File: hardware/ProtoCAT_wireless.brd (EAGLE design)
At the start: 59.7 x 53.3 mm, 69 parts, among them Q1 MOSFET-NCHANNELSMD, Q2 MOSFET-NCHANNELSMD, U1 ARDUINO, U3 TB6612FNG

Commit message: Numerous minor edits
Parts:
- added F3: PTCSMD, SparkFun-PowerIC:PTC-1206
- moved C2 20.7 mm to (30.5, 10.8), turned to 180 degrees
- moved FRAME1 15.3 mm to (-3.81, -10.2)
- moved LOGO4 7.41 mm to (58.4, 31.8)
- moved LOGO3 5.03 mm to (5.21, 1.52), turned to 0 degrees
- moved SJ2 3.95 mm to (33.1, 14.7), turned to 90 degrees
- moved LOGO1 2.84 mm to (14.9, 4.32)
- moved JP20 1.27 mm to (21.6, 8.00)
- moved C4 0.32 mm to (34.0, 26.7)
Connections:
- removed net FUSED_VCC: C2.1, F2.2, SJ1.3, SJ2.3, U3.19, U3.20
- removed net VCC: F2.1, R10.2, R13.2, U1.5V
- new net 5V: F2.1, U1.5V
- new net FUSED_3.3V: F3.2, JP23.2, MOD1.1, Q1.1, Q2.1, R11.2, R12.2, R6.1, R7.1, R9.2
- new net FUSED_5V: C2.1, F2.2, R10.2, R13.2, SJ1.3, SJ2.3, U3.19, U3.20
- net 3.3V: now also F3.1; no longer JP23.2, MOD1.1, Q1.1, Q2.1, R11.2, R12.2, R6.1, R7.1, R9.2
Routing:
- net 3.3V: track 97.4 -> 5.45 mm, vias 3 -> 0
- net FUSED_3.3V: track 0.00 -> 88.6 mm, vias 0 -> 1
- net FUSED_5V: track 0.00 -> 77.4 mm, vias 0 -> 2
- net FUSED_VCC: track 72.0 -> 0.00 mm, vias 3 -> 0
- net VCC: track 27.6 -> 0.00 mm, vias 2 -> 0
- net 5V: track 0.00 -> 5.52 mm
- net ANALOG_PWR_RAIL: track 18.9 -> 23.2 mm, vias 0 -> 1
- net FUSED_VIN: track 83.8 -> 86.7 mm, vias 6 -> 3
- net DIN: track 45.5 -> 42.8 mm
- net AOUT1: track 27.3 -> 29.4 mm
- net A0/SW_RXI: track 64.4 -> 62.5 mm
- net AIN1: track 25.8 -> 24.0 mm
- net AOUT2: track 41.2 -> 42.4 mm
- net D1_TXO: track 61.9 -> 60.7 mm
- net D0_RXI: track 73.4 -> 72.4 mm
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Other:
- board text added: "XBEE RESET"

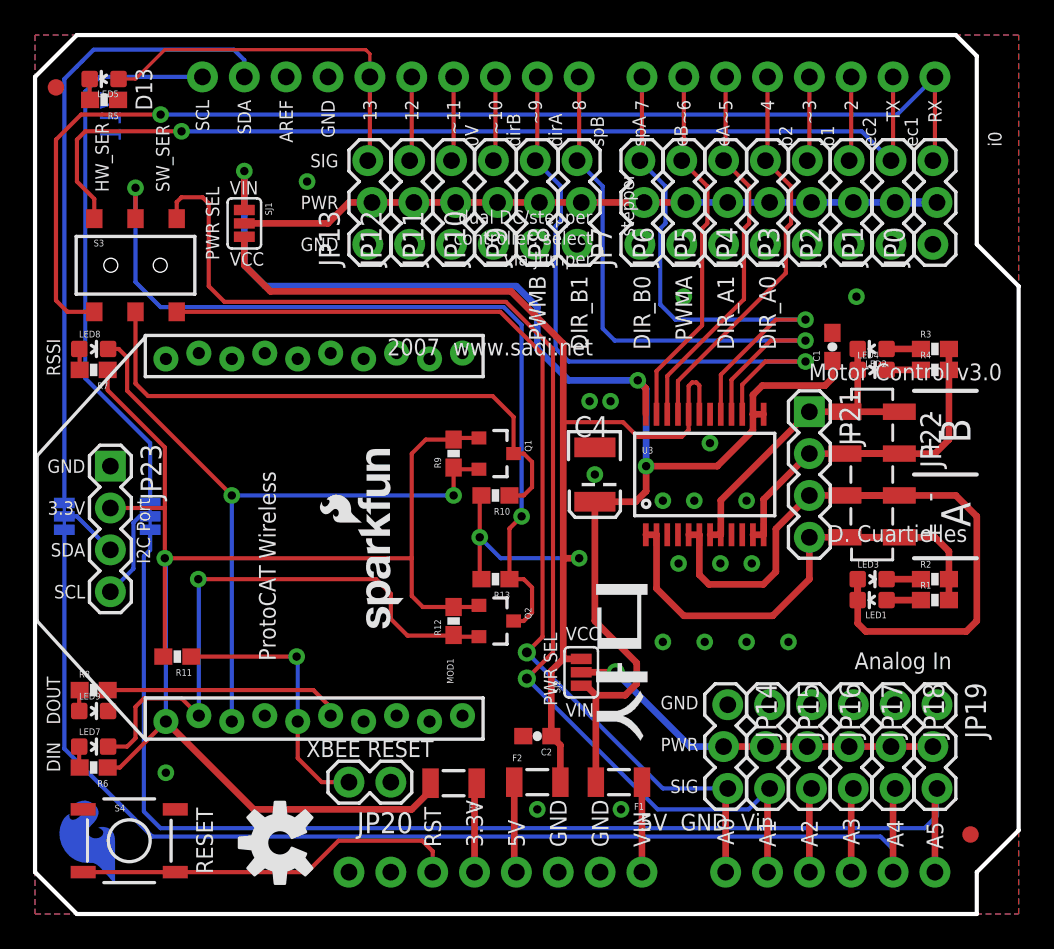
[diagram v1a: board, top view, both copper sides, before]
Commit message: Switched TX / RX lines on XBee
Fixed the Switched TX / RX lines from XBee to Arduino on the HW Serial
lines.

Moved the thru-hole mounts for the Motors to below the SMD mount.

Fixed LEDs for RSSI, DIN / DOUT
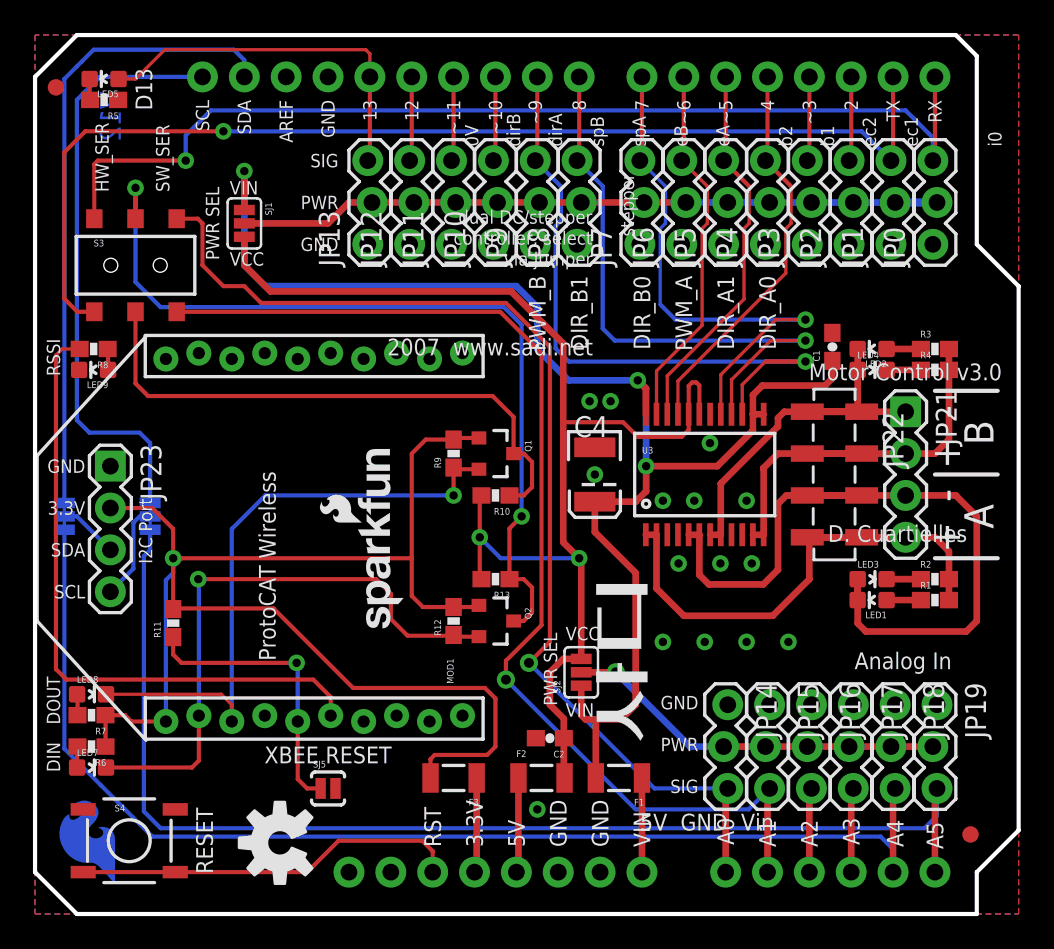
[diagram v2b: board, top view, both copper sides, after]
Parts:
- removed JP20: M02PTH, SparkFun-Connectors:1X02
- added SJ5: SOLDERJUMPERNO, SparkFun-Retired:SJ_2S-NO
- moved LOGO4 36.7 mm to (21.8, 28.8)
- moved R7 21.0 mm to (3.43, 12.1)
- moved LED8 21.0 mm to (3.43, 13.3)
- moved LED9 20.7 mm to (3.56, 33.0), turned to 90 degrees
- moved R8 20.7 mm to (3.56, 34.3), turned to 180 degrees
- moved JP21 5.84 mm to (52.8, 30.5)
- moved JP22 2.29 mm to (48.5, 30.5)
- moved R11 2.05 mm to (8.38, 17.7), turned to 90 degrees
- moved LED7 1.28 mm to (3.43, 8.89)
- moved R6 1.28 mm to (3.43, 10.2)
- moved C2 0.77 mm to (31.2, 10.7)
- moved F2 0.36 mm to (30.7, 8.26)
- moved F3 0.32 mm to (25.4, 8.26)
- moved F1 0.25 mm to (35.4, 8.26)
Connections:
- removed net D0_RXI: JP0.3, S3.4, U1.RX
- removed net D1_TXO: JP1.3, S3.1, U1.TX
- new net D0/RXI: JP0.3, S3.1, U1.RX
- new net D1/TXO: JP1.3, S3.4, U1.TX
- net A0/SW_RXI: now also S3.3; no longer S3.6
- net A1/SW_TXO: now also S3.6; no longer S3.3
- net GND: now also SJ5.2; no longer JP20.1
- net XBEE_RESET: now also SJ5.1; no longer JP20.2
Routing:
- net D0_RXI: track 72.4 -> 0.00 mm, vias 1 -> 0
- net D1/TXO: track 0.00 -> 67.6 mm, vias 0 -> 1
- net D0/RXI: track 0.00 -> 63.7 mm, vias 0 -> 1
- net D1_TXO: track 60.7 -> 0.00 mm, vias 1 -> 0
- net RSSI: track 14.5 -> 39.1 mm
- net A1/SW_TXO: track 75.1 -> 68.8 mm
- net A0/SW_RXI: track 62.5 -> 67.4 mm
- net DIN: track 42.8 -> 38.2 mm, vias 2 -> 1
- net BOUT2: track 17.1 -> 20.9 mm
- net SCL: track 34.1 -> 36.3 mm
- net FUSED_3.3V: track 88.6 -> 87.4 mm
- net FUSED_VIN: track 86.7 -> 87.9 mm
- net XBEE_RESET: track 16.3 -> 17.5 mm
- net BOUT1: track 21.0 -> 22.2 mm
- net AOUT2: track 42.4 -> 43.3 mm
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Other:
- board text added: "PWM_A"
- board text added: "PWM_B"
- board text added: "V12"
- board text removed: "PWMA"
- board text removed: "PWMB"
- board text removed: "V11"
